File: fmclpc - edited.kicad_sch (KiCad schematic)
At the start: 3 parts, among them J1401 ASP-134604-01, J1402 ASP-134604-01

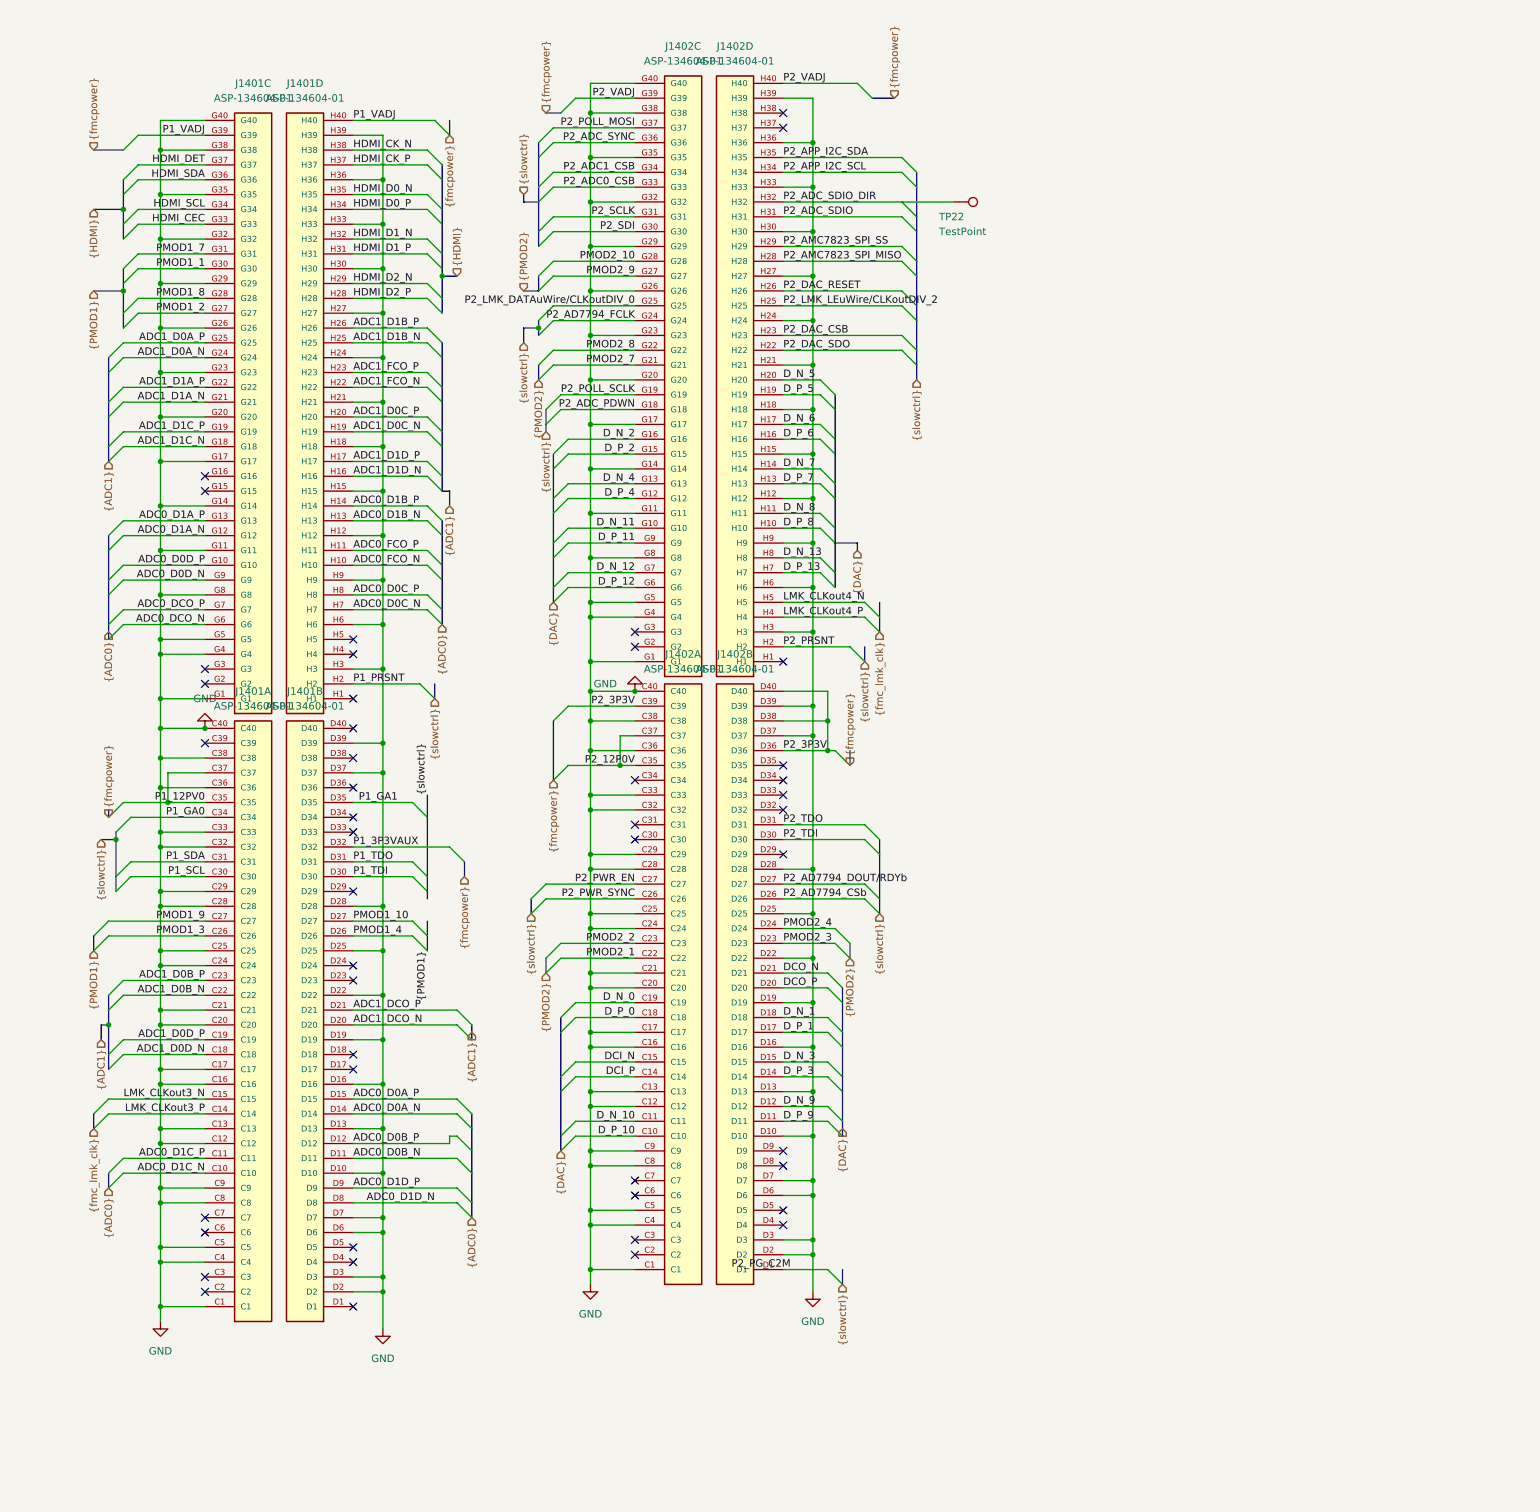
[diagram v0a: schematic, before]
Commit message: Schematic Changes
Added Manufacturer/MPN/Description Fields to parts
Added libraries to project
Modified FMC schematic to use new symbol
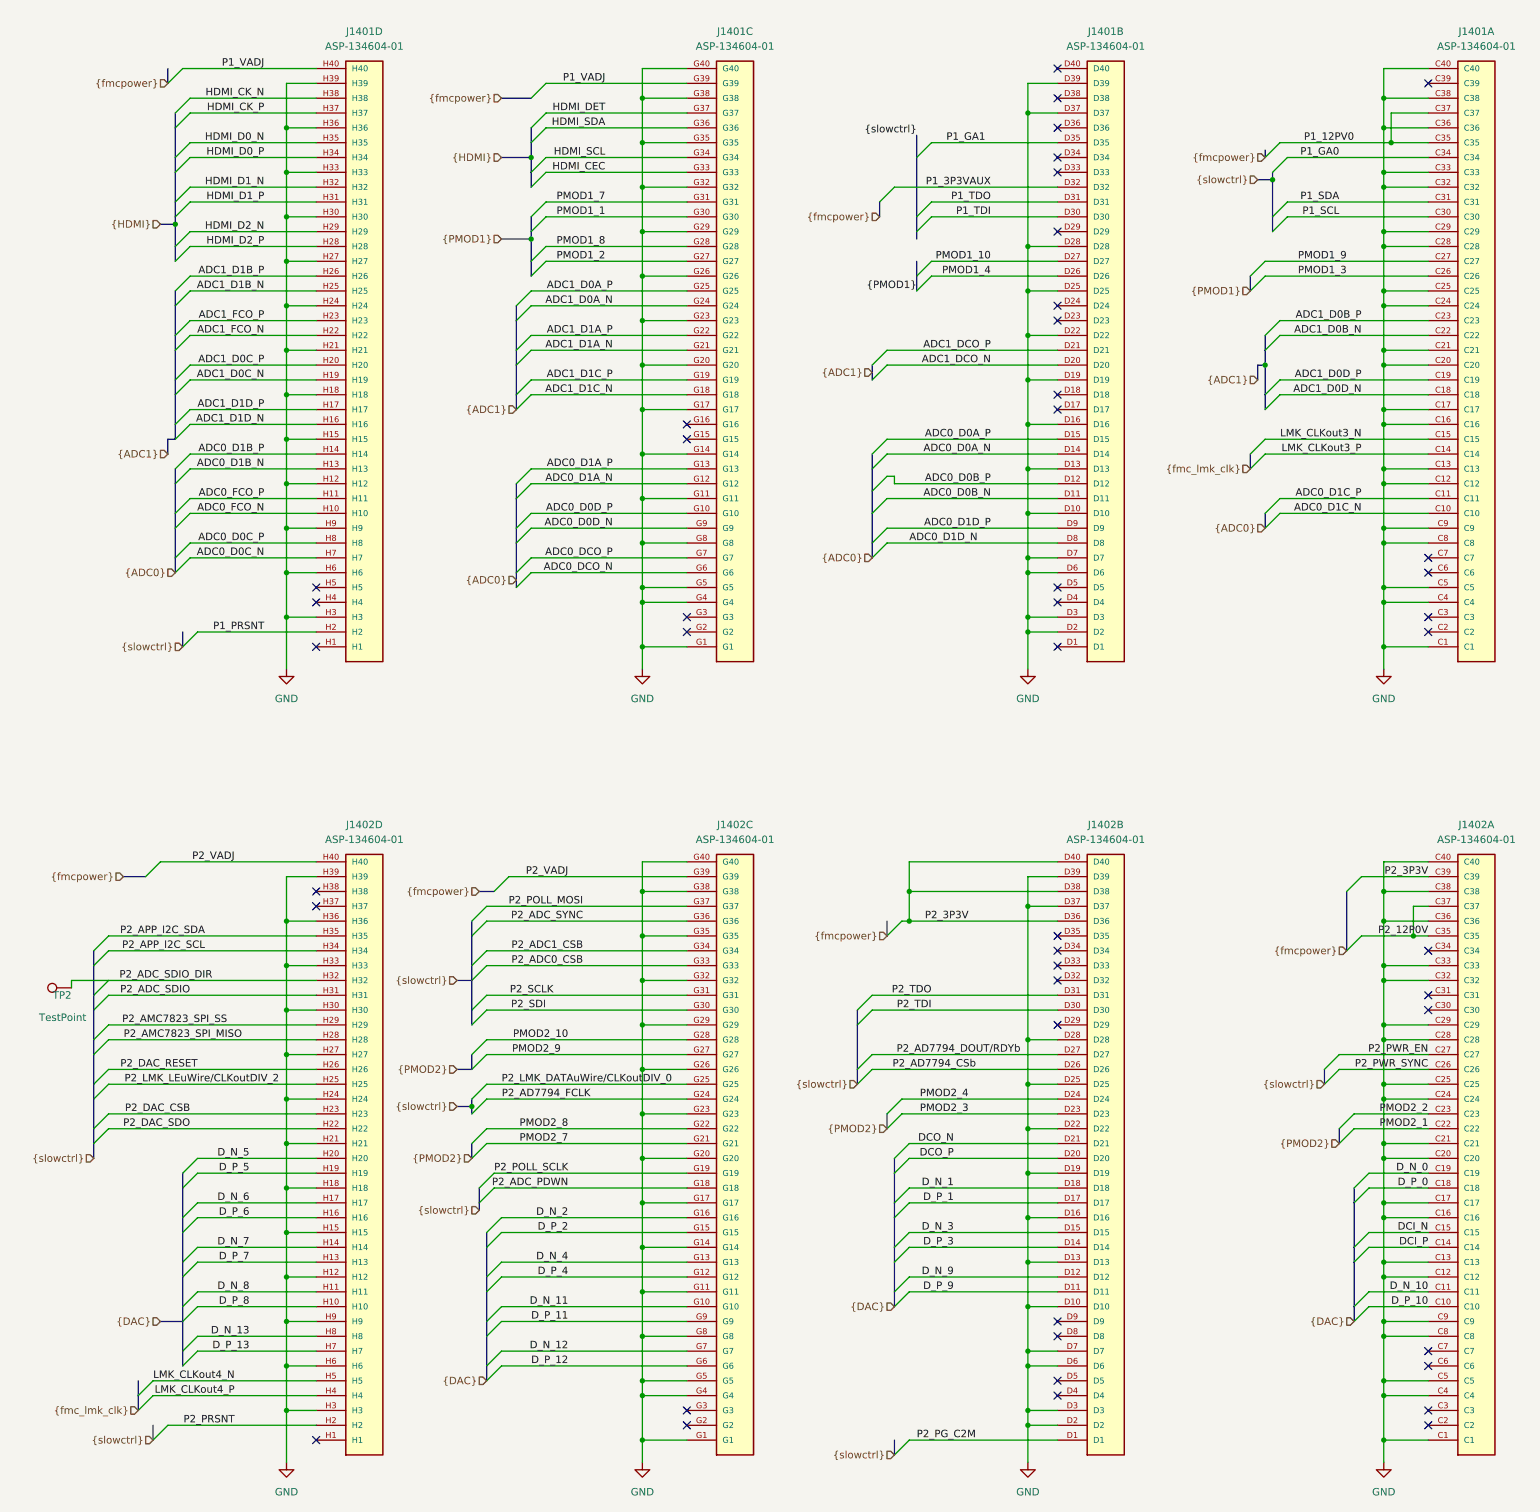
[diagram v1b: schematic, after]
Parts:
- removed TP22: TestPoint, 001_download:TestPoint_Pad_D0.6mm, symbol Connector:TestPoint
- added TP2: TestPoint, 001_download:TestPoint_Pad_D0.6mm, symbol Connector:TestPoint
- J1401, J1402: footprint 001_download:SAMTEC_ASP-134604-01 -> QuartzFootprints:SAMTEC_ASP-134604-01; MPN (none) -> ASP-134604-01; Manufacturer (none) -> Samtec Inc.
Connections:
- net P2_ADC_SDIO_DIR: now also TP2.1
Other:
- moved on the sheet: J1401A
